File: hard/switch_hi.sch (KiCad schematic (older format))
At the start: 5 parts

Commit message: pc format refactor wip
@lukekaese leds still need to be attenuated
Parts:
- gave numbers to parts that had none: 5

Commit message: layouting update
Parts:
- R1: renamed from R2; footprint Resistor_SMD:R_0603_1608Metric -> Resistor_SMD:R_0402_1005Metric
- R2: renamed from R3; footprint Resistor_SMD:R_0603_1608Metric -> Resistor_SMD:R_1210_3225Metric
- R3: renamed from R1; footprint Resistor_SMD:R_0603_1608Metric -> Resistor_SMD:R_0402_1005Metric
- renumbered M2 to M1, M1 to M2

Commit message: driver nmos update
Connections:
- net +5V: now also M1.3 (D); no longer R2.1
- net ANODES: now also R2.2; no longer M1.2 (S)
- new net: M1.2 (S), R2.1
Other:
- moved on the sheet: R17
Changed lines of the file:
@@
 $Descr A4 11693 8268
 encoding utf-8
-Sheet 4 69
+Sheet 9 69
 Title ""
 Date ""
@@
 AR Path="/6053C67A/A575BEE6/93A487A2" Ref="M61"  Part="1"
 AR Path="/6053C67A/A575BEEA/93A487A2" Ref="M63"  Part="1"
-F 0 "M1" H 6228 3850 50  0000 L CNN
+F 0 "M11" H 6228 3850 50  0000 L CNN
 F 1 "IRLML6402TRPBF" H 6228 3805 50  0001 L CNN
 F 2 "Package_TO_SOT_SMD:SOT-23" H 7250 3850 50  0001 C CNN
@@
 L Device:R R?
 U 1 1 93A487A8
-P 6150 3450
+P 6150 4250
 AR Path="/6053C67A/93A487A8" Ref="R?"  Part="1"
 AR Path="/6053C67A/912BCC0B/93A487A8" Ref="R2"  Part="1"
@@
 AR Path="/6053C67A/A575BEE6/93A487A8" Ref="R92"  Part="1"
 AR Path="/6053C67A/A575BEEA/93A487A8" Ref="R95"  Part="1"
-F 0 "R2" H 6220 3496 50  0000 L CNN
-F 1 "120R" H 6220 3405 50  0000 L CNN
-F 2 "Resistor_SMD:R_1210_3225Metric" V 6080 3450 50  0001 C CNN
-F 3 "~" H 6150 3450 50  0001 C CNN
-	1    6150 3450
+F 0 "R17" H 6220 4296 50  0000 L CNN
+F 1 "120R" H 6220 4205 50  0000 L CNN
+F 2 "Resistor_SMD:R_1210_3225Metric" V 6080 4250 50  0001 C CNN
+F 3 "~" H 6150 4250 50  0001 C CNN
+	1    6150 4250
 	1    0    0    -1
 $EndComp
@@
 AR Path="/6053C67A/A575BEE6/93A487AE" Ref="R91"  Part="1"
 AR Path="/6053C67A/A575BEEA/93A487AE" Ref="R94"  Part="1"
-F 0 "R1" H 5820 3496 50  0000 L CNN
+F 0 "R16" H 5820 3496 50  0000 L CNN
 F 1 "1K" H 5820 3405 50  0000 L CNN
 F 2 "Resistor_SMD:R_0402_1005Metric" V 5680 3450 50  0001 C CNN
@@
 AR Path="/6053C67A/A575BEE6/93A487B8" Ref="M62"  Part="1"
 AR Path="/6053C67A/A575BEEA/93A487B8" Ref="M64"  Part="1"
-F 0 "M2" H 5828 4100 50  0000 L CNN
+F 0 "M12" H 5828 4100 50  0000 L CNN
 F 1 "2N7002,215" H 5828 4055 50  0001 L CNN
 F 2 "Package_TO_SOT_SMD:SOT-23" H 6500 4100 50  0001 C CNN
@@
 AR Path="/6053C67A/A575BEE6/93A487BE" Ref="R93"  Part="1"
 AR Path="/6053C67A/A575BEEA/93A487BE" Ref="R96"  Part="1"
-F 0 "R3" V 5043 4100 50  0000 C CNN
+F 0 "R18" V 5043 4100 50  0000 C CNN
 F 1 "1K8" V 5134 4100 50  0000 C CNN
 F 2 "Resistor_SMD:R_0402_1005Metric" V 5180 4100 50  0001 C CNN
@@
 Wire Wire Line
 	5850 3850 5750 3850
-Wire Wire Line
-	6150 3600 6150 3650
 Wire Wire Line
 	5400 4100 5450 4100
@@
 AR Path="/6053C67A/A575BEE6/93A487CA" Ref="#PWR0110"  Part="1"
 AR Path="/6053C67A/A575BEEA/93A487CA" Ref="#PWR0113"  Part="1"
-F 0 "#PWR020" H 5750 4100 50  0001 C CNN
+F 0 "#PWR035" H 5750 4100 50  0001 C CNN
 F 1 "GND" H 5755 4177 50  0000 C CNN
 F 2 "" H 5750 4350 50  0001 C CNN
@@
 AR Path="/6053C67A/A575BEE6/93A5160E" Ref="#PWR0108"  Part="1"
 AR Path="/6053C67A/A575BEEA/93A5160E" Ref="#PWR0111"  Part="1"
-F 0 "#PWR018" H 5750 3100 50  0001 C CNN
+F 0 "#PWR033" H 5750 3100 50  0001 C CNN
 F 1 "+5V" H 5765 3423 50  0000 C CNN
 F 2 "" H 5750 3250 50  0001 C CNN
@@
 	5750 3900 5750 3850
 Connection ~ 5750 3850
-Wire Wire Line
-	6150 3300 6150 3250
 $Comp
 L power:+5V #PWR019
 U 1 1 93A5098C
-P 6150 3250
+P 6150 3600
 AR Path="/6053C67A/912BCC0B/93A5098C" Ref="#PWR019"  Part="1"
 AR Path="/6053C67A/9C96A33F/93A5098C" Ref="#PWR?"  Part="1"
@@
 AR Path="/6053C67A/A575BEE6/93A5098C" Ref="#PWR0109"  Part="1"
 AR Path="/6053C67A/A575BEEA/93A5098C" Ref="#PWR0112"  Part="1"
-F 0 "#PWR019" H 6150 3100 50  0001 C CNN
-F 1 "+5V" H 6165 3423 50  0000 C CNN
-F 2 "" H 6150 3250 50  0001 C CNN
-F 3 "" H 6150 3250 50  0001 C CNN
-	1    6150 3250
+F 0 "#PWR034" H 6150 3450 50  0001 C CNN
+F 1 "+5V" H 6165 3773 50  0000 C CNN
+F 2 "" H 6150 3600 50  0001 C CNN
+F 3 "" H 6150 3600 50  0001 C CNN
+	1    6150 3600
 	1    0    0    -1
 $EndComp
@@
 Wire Wire Line
 	6150 4050 6150 4100
-Text HLabel 6150 4100 3    50   Output ~ 0
+Text HLabel 6150 4450 3    50   Output ~ 0
 ANODES
+Wire Wire Line
+	6150 4450 6150 4400
+Wire Wire Line
+	6150 3650 6150 3600
 $EndSCHEMATC

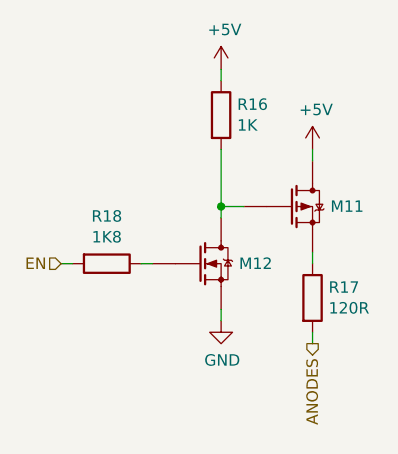
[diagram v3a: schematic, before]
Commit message: uc minimum application
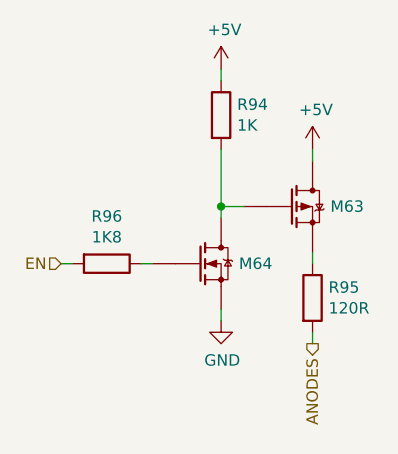
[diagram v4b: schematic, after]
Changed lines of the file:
@@
 $Descr A4 11693 8268
 encoding utf-8
-Sheet 9 69
+Sheet 6 69
 Title ""
 Date ""
@@
 AR Path="/6053C67A/A575BEE6/93A487A2" Ref="M61"  Part="1"
 AR Path="/6053C67A/A575BEEA/93A487A2" Ref="M63"  Part="1"
-F 0 "M11" H 6228 3850 50  0000 L CNN
+F 0 "M63" H 6228 3850 50  0000 L CNN
 F 1 "IRLML6402TRPBF" H 6228 3805 50  0001 L CNN
 F 2 "Package_TO_SOT_SMD:SOT-23" H 7250 3850 50  0001 C CNN
@@
 AR Path="/6053C67A/A575BEE6/93A487A8" Ref="R92"  Part="1"
 AR Path="/6053C67A/A575BEEA/93A487A8" Ref="R95"  Part="1"
-F 0 "R17" H 6220 4296 50  0000 L CNN
+F 0 "R95" H 6220 4296 50  0000 L CNN
 F 1 "120R" H 6220 4205 50  0000 L CNN
 F 2 "Resistor_SMD:R_1210_3225Metric" V 6080 4250 50  0001 C CNN
@@
 AR Path="/6053C67A/A575BEE6/93A487AE" Ref="R91"  Part="1"
 AR Path="/6053C67A/A575BEEA/93A487AE" Ref="R94"  Part="1"
-F 0 "R16" H 5820 3496 50  0000 L CNN
+F 0 "R94" H 5820 3496 50  0000 L CNN
 F 1 "1K" H 5820 3405 50  0000 L CNN
 F 2 "Resistor_SMD:R_0402_1005Metric" V 5680 3450 50  0001 C CNN
@@
 AR Path="/6053C67A/A575BEE6/93A487B8" Ref="M62"  Part="1"
 AR Path="/6053C67A/A575BEEA/93A487B8" Ref="M64"  Part="1"
-F 0 "M12" H 5828 4100 50  0000 L CNN
+F 0 "M64" H 5828 4100 50  0000 L CNN
 F 1 "2N7002,215" H 5828 4055 50  0001 L CNN
 F 2 "Package_TO_SOT_SMD:SOT-23" H 6500 4100 50  0001 C CNN
@@
 AR Path="/6053C67A/A575BEE6/93A487BE" Ref="R93"  Part="1"
 AR Path="/6053C67A/A575BEEA/93A487BE" Ref="R96"  Part="1"
-F 0 "R18" V 5043 4100 50  0000 C CNN
+F 0 "R96" V 5043 4100 50  0000 C CNN
 F 1 "1K8" V 5134 4100 50  0000 C CNN
 F 2 "Resistor_SMD:R_0402_1005Metric" V 5180 4100 50  0001 C CNN
@@
 AR Path="/6053C67A/A575BEE6/93A487CA" Ref="#PWR0110"  Part="1"
 AR Path="/6053C67A/A575BEEA/93A487CA" Ref="#PWR0113"  Part="1"
-F 0 "#PWR035" H 5750 4100 50  0001 C CNN
+F 0 "#PWR0113" H 5750 4100 50  0001 C CNN
 F 1 "GND" H 5755 4177 50  0000 C CNN
 F 2 "" H 5750 4350 50  0001 C CNN
@@
 AR Path="/6053C67A/A575BEE6/93A5160E" Ref="#PWR0108"  Part="1"
 AR Path="/6053C67A/A575BEEA/93A5160E" Ref="#PWR0111"  Part="1"
-F 0 "#PWR033" H 5750 3100 50  0001 C CNN
+F 0 "#PWR0111" H 5750 3100 50  0001 C CNN
 F 1 "+5V" H 5765 3423 50  0000 C CNN
 F 2 "" H 5750 3250 50  0001 C CNN
@@
 AR Path="/6053C67A/A575BEE6/93A5098C" Ref="#PWR0109"  Part="1"
 AR Path="/6053C67A/A575BEEA/93A5098C" Ref="#PWR0112"  Part="1"
-F 0 "#PWR034" H 6150 3450 50  0001 C CNN
+F 0 "#PWR0112" H 6150 3450 50  0001 C CNN
 F 1 "+5V" H 6165 3773 50  0000 C CNN
 F 2 "" H 6150 3600 50  0001 C CNN

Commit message: pcb format refactor
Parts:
- renumbered M1 to M2, M2 to M3, R1 to R11, R3 to R12, R2 to R13

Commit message: layout progress
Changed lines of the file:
@@
 $Descr A4 11693 8268
 encoding utf-8
-Sheet 6 69
+Sheet 4 69
 Title ""
 Date ""
@@
 AR Path="/6053C67A/A575BEE6/93A487A2" Ref="M62"  Part="1"
 AR Path="/6053C67A/A575BEEA/93A487A2" Ref="M64"  Part="1"
-F 0 "M64" H 6228 3850 50  0000 L CNN
+F 0 "M2" H 6228 3850 50  0000 L CNN
 F 1 "IRLML6402TRPBF" H 6228 3805 50  0001 L CNN
 F 2 "Package_TO_SOT_SMD:SOT-23" H 7250 3850 50  0001 C CNN
@@
 AR Path="/6053C67A/A575BEE6/93A487A8" Ref="R103"  Part="1"
 AR Path="/6053C67A/A575BEEA/93A487A8" Ref="R106"  Part="1"
-F 0 "R106" H 6220 4296 50  0000 L CNN
+F 0 "R13" H 6220 4296 50  0000 L CNN
 F 1 "120R" H 6220 4205 50  0000 L CNN
 F 2 "Resistor_SMD:R_1210_3225Metric" V 6080 4250 50  0001 C CNN
@@
 AR Path="/6053C67A/A575BEE6/93A487AE" Ref="R101"  Part="1"
 AR Path="/6053C67A/A575BEEA/93A487AE" Ref="R104"  Part="1"
-F 0 "R104" H 5820 3496 50  0000 L CNN
+F 0 "R11" H 5820 3496 50  0000 L CNN
 F 1 "1K" H 5820 3405 50  0000 L CNN
 F 2 "Resistor_SMD:R_0402_1005Metric" V 5680 3450 50  0001 C CNN
@@
 AR Path="/6053C67A/A575BEE6/93A487B8" Ref="M63"  Part="1"
 AR Path="/6053C67A/A575BEEA/93A487B8" Ref="M65"  Part="1"
-F 0 "M65" H 5828 4100 50  0000 L CNN
+F 0 "M3" H 5828 4100 50  0000 L CNN
 F 1 "2N7002,215" H 5828 4055 50  0001 L CNN
 F 2 "Package_TO_SOT_SMD:SOT-23" H 6500 4100 50  0001 C CNN
@@
 AR Path="/6053C67A/A575BEE6/93A487BE" Ref="R102"  Part="1"
 AR Path="/6053C67A/A575BEEA/93A487BE" Ref="R105"  Part="1"
-F 0 "R105" V 5043 4100 50  0000 C CNN
+F 0 "R12" V 5043 4100 50  0000 C CNN
 F 1 "1K8" V 5134 4100 50  0000 C CNN
 F 2 "Resistor_SMD:R_0402_1005Metric" V 5180 4100 50  0001 C CNN

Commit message: layout progress
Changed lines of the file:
@@
 $Descr A4 11693 8268
 encoding utf-8
-Sheet 4 69
+Sheet 24 69
 Title ""
 Date ""
@@
 AR Path="/6053C67A/A575BEE6/93A487A2" Ref="M62"  Part="1"
 AR Path="/6053C67A/A575BEEA/93A487A2" Ref="M64"  Part="1"
-F 0 "M2" H 6228 3850 50  0000 L CNN
+F 0 "M42" H 6228 3850 50  0000 L CNN
 F 1 "IRLML6402TRPBF" H 6228 3805 50  0001 L CNN
 F 2 "Package_TO_SOT_SMD:SOT-23" H 7250 3850 50  0001 C CNN
@@
 AR Path="/6053C67A/A575BEE6/93A487A8" Ref="R103"  Part="1"
 AR Path="/6053C67A/A575BEEA/93A487A8" Ref="R106"  Part="1"
-F 0 "R13" H 6220 4296 50  0000 L CNN
+F 0 "R73" H 6220 4296 50  0000 L CNN
 F 1 "120R" H 6220 4205 50  0000 L CNN
 F 2 "Resistor_SMD:R_1210_3225Metric" V 6080 4250 50  0001 C CNN
@@
 AR Path="/6053C67A/A575BEE6/93A487AE" Ref="R101"  Part="1"
 AR Path="/6053C67A/A575BEEA/93A487AE" Ref="R104"  Part="1"
-F 0 "R11" H 5820 3496 50  0000 L CNN
+F 0 "R71" H 5820 3496 50  0000 L CNN
 F 1 "1K" H 5820 3405 50  0000 L CNN
 F 2 "Resistor_SMD:R_0402_1005Metric" V 5680 3450 50  0001 C CNN
@@
 AR Path="/6053C67A/A575BEE6/93A487B8" Ref="M63"  Part="1"
 AR Path="/6053C67A/A575BEEA/93A487B8" Ref="M65"  Part="1"
-F 0 "M3" H 5828 4100 50  0000 L CNN
+F 0 "M43" H 5828 4100 50  0000 L CNN
 F 1 "2N7002,215" H 5828 4055 50  0001 L CNN
 F 2 "Package_TO_SOT_SMD:SOT-23" H 6500 4100 50  0001 C CNN
@@
 AR Path="/6053C67A/A575BEE6/93A487BE" Ref="R102"  Part="1"
 AR Path="/6053C67A/A575BEEA/93A487BE" Ref="R105"  Part="1"
-F 0 "R12" V 5043 4100 50  0000 C CNN
+F 0 "R72" V 5043 4100 50  0000 C CNN
 F 1 "1K8" V 5134 4100 50  0000 C CNN
 F 2 "Resistor_SMD:R_0402_1005Metric" V 5180 4100 50  0001 C CNN

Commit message: release candidate. ready for review by @lukekaese
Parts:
- R13: value 120R -> 0R
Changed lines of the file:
@@
 $Descr A4 11693 8268
 encoding utf-8
-Sheet 24 69
-Title ""
-Date ""
-Rev ""
-Comp ""
+Sheet 18 70
+Title "LED Matrix V3"
+Date "2021-03-23"
+Rev "0"
+Comp "F2A"
 Comment1 ""
 Comment2 ""
@@
 AR Path="/6053C67A/A575BEE6/93A487A2" Ref="M62"  Part="1"
 AR Path="/6053C67A/A575BEEA/93A487A2" Ref="M64"  Part="1"
-F 0 "M42" H 6228 3850 50  0000 L CNN
+F 0 "M30" H 6228 3850 50  0000 L CNN
 F 1 "IRLML6402TRPBF" H 6228 3805 50  0001 L CNN
 F 2 "Package_TO_SOT_SMD:SOT-23" H 7250 3850 50  0001 C CNN
@@
 AR Path="/6053C67A/A575BEE6/93A487A8" Ref="R103"  Part="1"
 AR Path="/6053C67A/A575BEEA/93A487A8" Ref="R106"  Part="1"
-F 0 "R73" H 6220 4296 50  0000 L CNN
-F 1 "120R" H 6220 4205 50  0000 L CNN
+F 0 "R55" H 6220 4296 50  0000 L CNN
+F 1 "0R" H 6220 4205 50  0000 L CNN
 F 2 "Resistor_SMD:R_1210_3225Metric" V 6080 4250 50  0001 C CNN
 F 3 "~" H 6150 4250 50  0001 C CNN
@@
 AR Path="/6053C67A/A575BEE6/93A487AE" Ref="R101"  Part="1"
 AR Path="/6053C67A/A575BEEA/93A487AE" Ref="R104"  Part="1"
-F 0 "R71" H 5820 3496 50  0000 L CNN
+F 0 "R53" H 5820 3496 50  0000 L CNN
 F 1 "1K" H 5820 3405 50  0000 L CNN
 F 2 "Resistor_SMD:R_0402_1005Metric" V 5680 3450 50  0001 C CNN
@@
 AR Path="/6053C67A/A575BEE6/93A487B8" Ref="M63"  Part="1"
 AR Path="/6053C67A/A575BEEA/93A487B8" Ref="M65"  Part="1"
-F 0 "M43" H 5828 4100 50  0000 L CNN
+F 0 "M31" H 5828 4100 50  0000 L CNN
 F 1 "2N7002,215" H 5828 4055 50  0001 L CNN
 F 2 "Package_TO_SOT_SMD:SOT-23" H 6500 4100 50  0001 C CNN
@@
 AR Path="/6053C67A/A575BEE6/93A487BE" Ref="R102"  Part="1"
 AR Path="/6053C67A/A575BEEA/93A487BE" Ref="R105"  Part="1"
-F 0 "R72" V 5043 4100 50  0000 C CNN
+F 0 "R54" V 5043 4100 50  0000 C CNN
 F 1 "1K8" V 5134 4100 50  0000 C CNN
 F 2 "Resistor_SMD:R_0402_1005Metric" V 5180 4100 50  0001 C CNN
